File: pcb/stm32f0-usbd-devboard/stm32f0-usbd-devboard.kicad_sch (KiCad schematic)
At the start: 28 parts, among them J1 USB_B_Mini, J2 PIN H 5P, J3 LEFT, J4 RIGHT, J5 BOOTLOADER, U1 USBLC6-2SC6, U2 MCP1700-3302E, U3 STM32F042K4T6 or STM32F042K6T6, Y1 8MHz

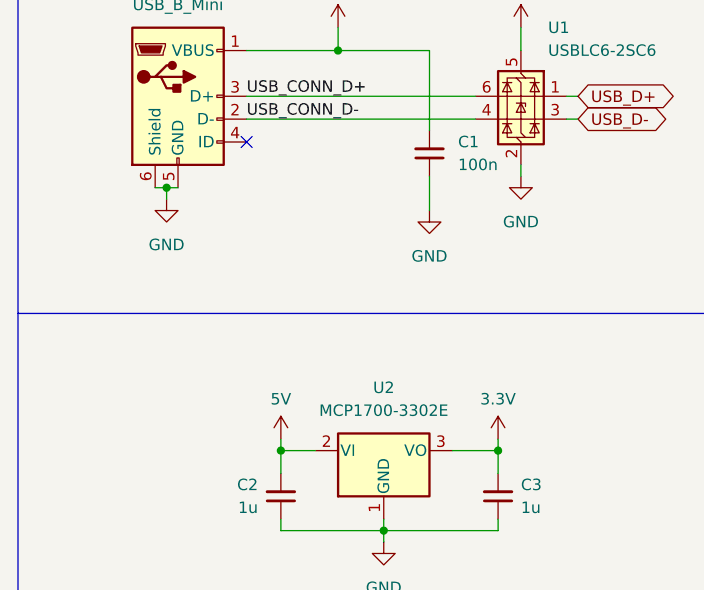
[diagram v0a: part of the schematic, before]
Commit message: pcb: f0: upgrade to kicad 10
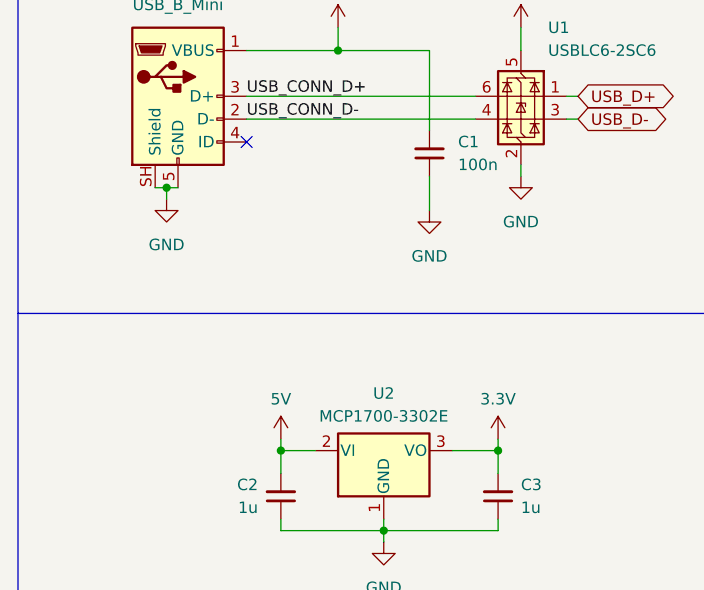
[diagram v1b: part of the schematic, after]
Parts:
- U2: symbol Regulator_Linear:MCP1700x-330xxTO -> custom:MCP1700x-330xxTO
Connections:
- net GND: now also J1.SH (Shield); no longer J1.6 (Shield)
